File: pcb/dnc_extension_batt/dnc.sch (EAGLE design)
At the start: 105 parts, among them Q1 IRF9321PBF, Q2 IRF9321PBF, Q3 BSS138, Q5 BSS138, U1 LCD-16X2NOHOLES, U2 74HCT595D

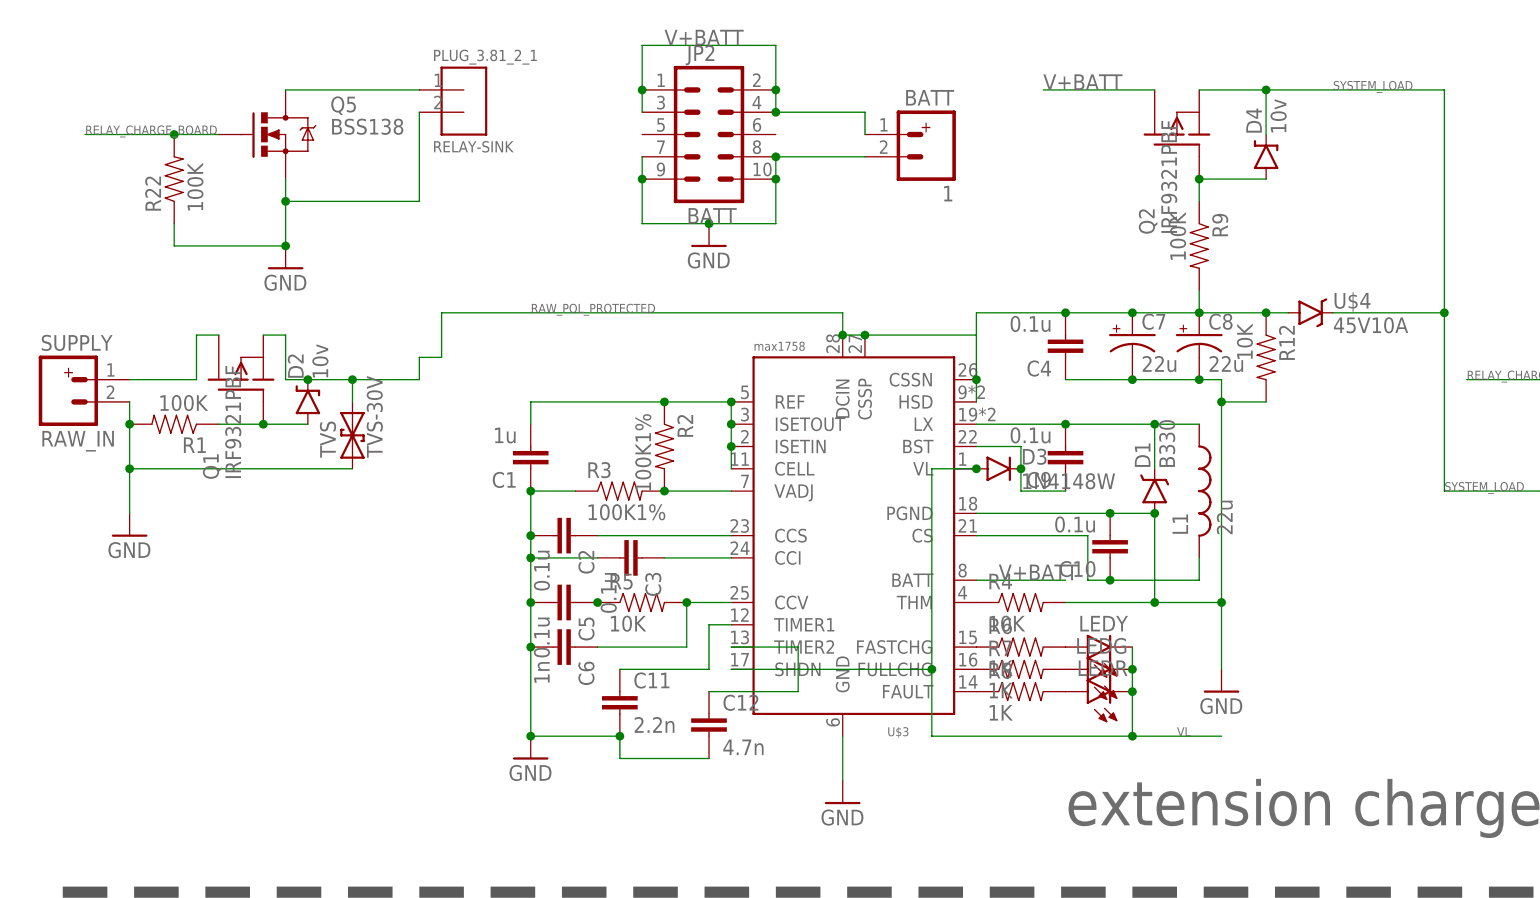
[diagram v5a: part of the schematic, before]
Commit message: major changes : - carte pieuvre - carte relais - correctif v1 : usb + pin A7 ! - enclosure
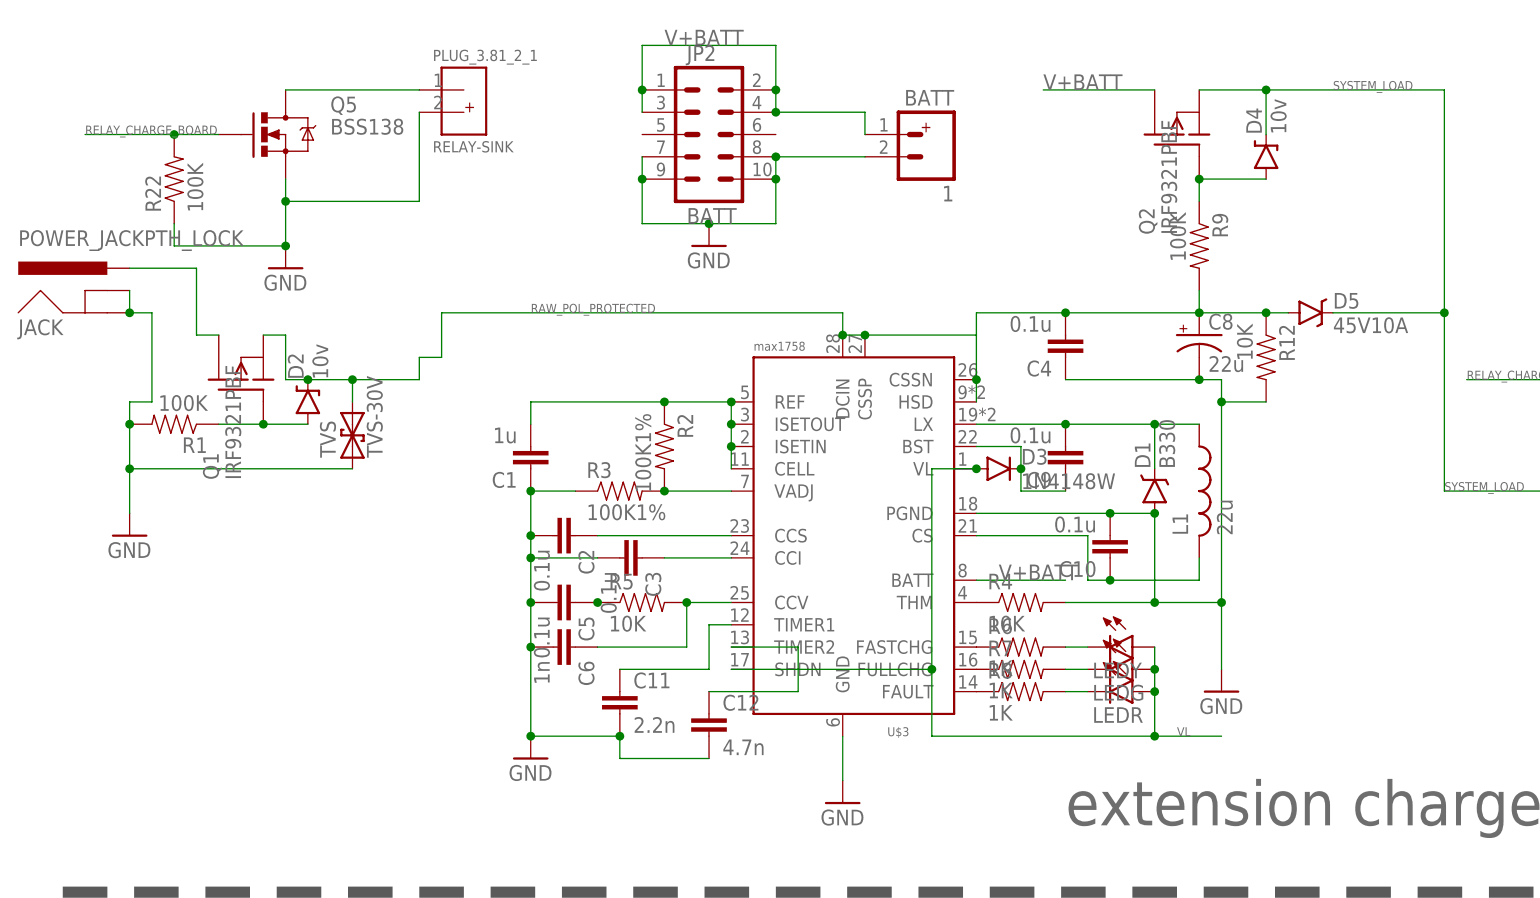
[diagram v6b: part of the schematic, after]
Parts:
- removed C7: 22u, SparkFun-Passives:CAP_POL1206
- removed RAW_IN: SUPPLY, pierre_vv:DNC_IN2PWR
- added JACK: POWER_JACKPTH_LOCK, SparkFun:POWER_JACKPTH_LOCK
- C8: device SparkFun-Passives:CAP_POL1206 -> SparkFun-Passives:CAP_POLC
- renumbered U$4 to D5
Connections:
- net GND: now also 1.-, JACK.GND, JACK.GNDBREAK; no longer 1.2, C7.-, RAW_IN.2
- net N$13: now also LEDY.C; no longer LEDY.A
- net N$14: now also LEDG.C; no longer LEDG.A
- net N$15: now also LEDR.C; no longer LEDR.A
- net RAW_POL_PROTECTED: no longer C7.+
- net RAW_UNPROTECTED1: now also JACK.PWR; no longer RAW_IN.1
- net V+BATT: now also 1.+; no longer 1.1
- net VL: now also LEDG.A, LEDR.A, LEDY.A; no longer LEDG.C, LEDR.C, LEDY.C
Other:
- moved on the sheet: LEDG, LEDR, LEDY
